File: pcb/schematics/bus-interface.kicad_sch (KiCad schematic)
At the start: 46 parts, among them J3 Conn_01x06, J4 Conn_01x06, U3 LCMXO2-1200HC-4TG100I

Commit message: add decoupling caps on bus controller
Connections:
- net +3V3: now also U3.93 (VCCIO0)
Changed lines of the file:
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@@
   (junction (at 82.55 44.45) (diameter 0) (color 0 0 0 0)
   )
+  (junction (at 134.62 36.83) (diameter 0) (color 0 0 0 0)
+  )
   (junction (at 241.3 49.53) (diameter 0) (color 0 0 0 0)
   )
@@
     (stroke (width 0) (type default))
   )
+  (wire (pts (xy 134.62 39.37) (xy 134.62 36.83))
+    (stroke (width 0) (type default))
+  )
   (wire (pts (xy 38.1 92.71) (xy 38.1 96.52))
     (stroke (width 0) (type default))
@@
     (stroke (width 0) (type default))
   )
-  (wire (pts (xy 133.35 36.83) (xy 149.86 36.83))
+  (wire (pts (xy 133.35 36.83) (xy 134.62 36.83))
     (stroke (width 0) (type default))
   )
@@
     (stroke (width 0) (type default))
   )
+  (wire (pts (xy 133.35 39.37) (xy 134.62 39.37))
+    (stroke (width 0) (type default))
+  )
   (wire (pts (xy 177.8 62.23) (xy 177.8 60.96))
     (stroke (width 0) (type default))
@@
     (stroke (width 0) (type default))
   )
+  (wire (pts (xy 134.62 36.83) (xy 149.86 36.83))
+    (stroke (width 0) (type default))
+  )

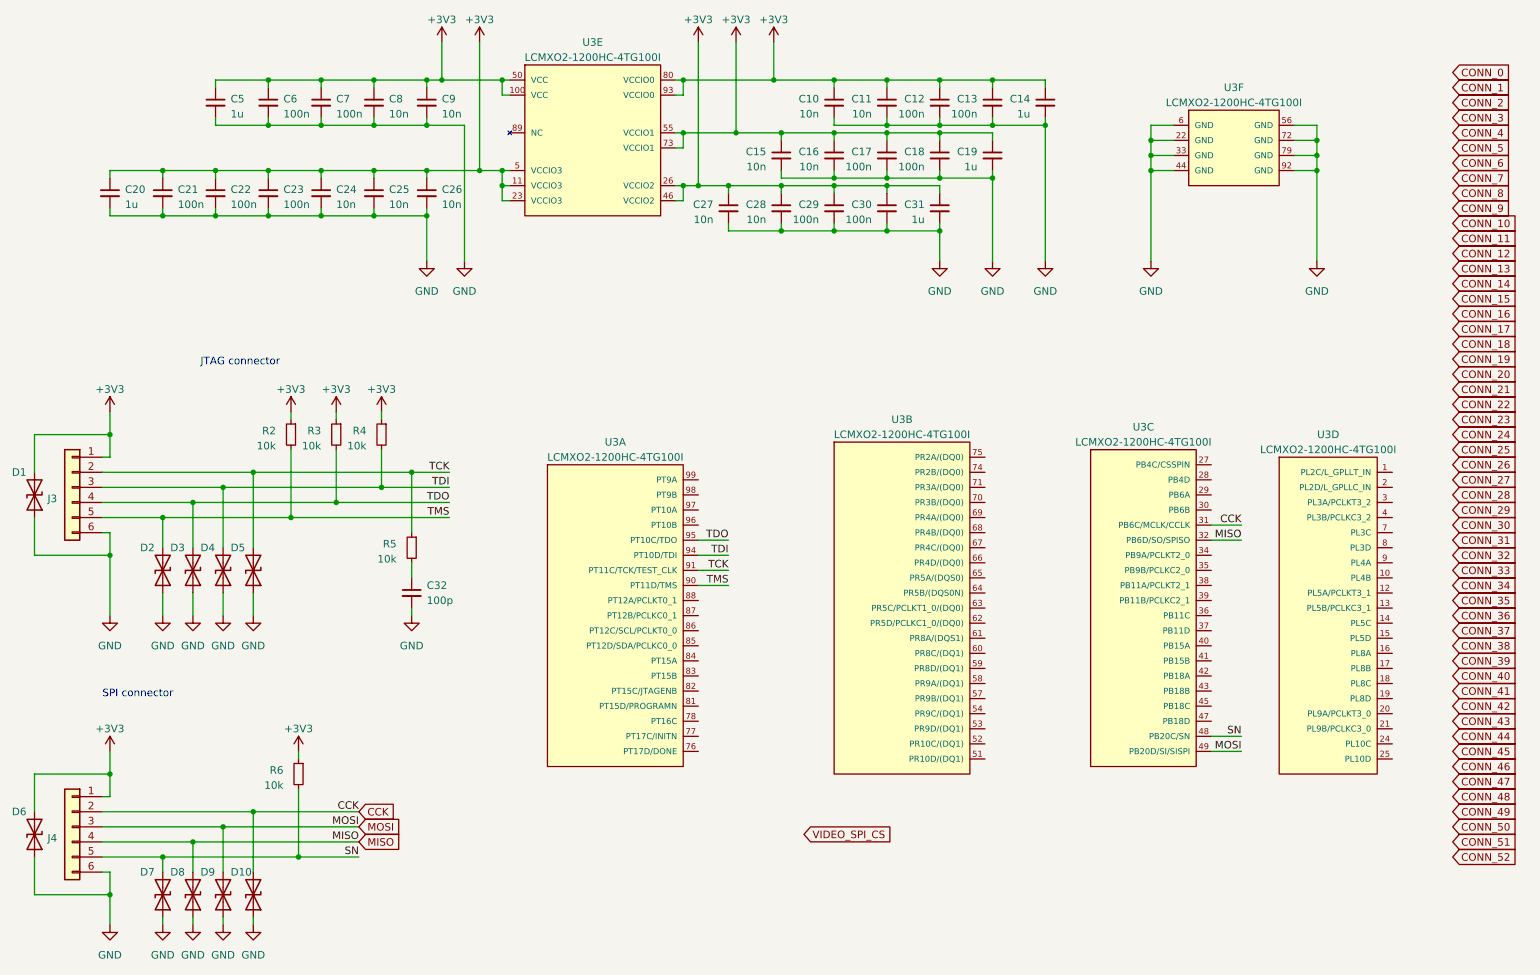
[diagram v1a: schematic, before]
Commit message: add traces from bus to bus controller
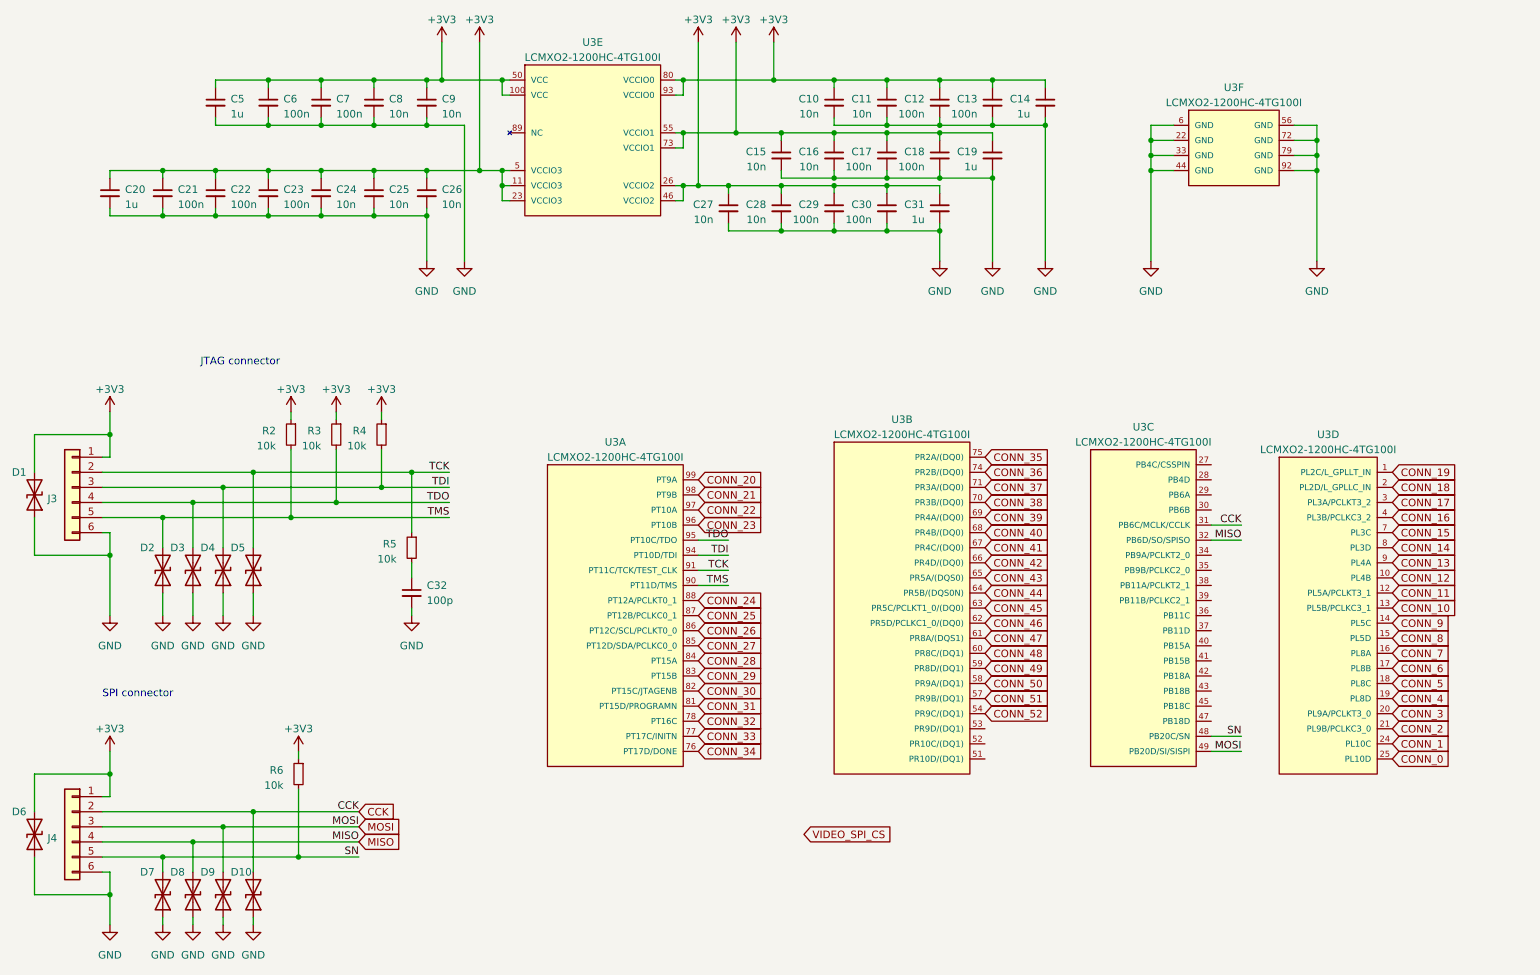
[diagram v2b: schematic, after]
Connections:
- net CONN_0: now also U3.25 (PL10D)
- net CONN_1: now also U3.24 (PL10C)
- net CONN_10: now also U3.13 (PL5B/PCLKC3_1)
- net CONN_11: now also U3.12 (PL5A/PCLKT3_1)
- net CONN_12: now also U3.10 (PL4B)
- net CONN_13: now also U3.9 (PL4A)
- net CONN_14: now also U3.8 (PL3D)
- net CONN_15: now also U3.7 (PL3C)
- net CONN_16: now also U3.4 (PL3B/PCLKC3_2)
- net CONN_17: now also U3.3 (PL3A/PCLKT3_2)
- net CONN_18: now also U3.2 (PL2D/L_GPLLC_IN)
- net CONN_19: now also U3.1 (PL2C/L_GPLLT_IN)
- net CONN_2: now also U3.21 (PL9B/PCLKC3_0)
- net CONN_20: now also U3.99 (PT9A)
- net CONN_21: now also U3.98 (PT9B)
- net CONN_22: now also U3.97 (PT10A)
- net CONN_23: now also U3.96 (PT10B)
- net CONN_24: now also U3.88 (PT12A/PCLKT0_1)
- net CONN_25: now also U3.87 (PT12B/PCLKC0_1)
- net CONN_26: now also U3.86 (PT12C/SCL/PCLKT0_0)
- net CONN_27: now also U3.85 (PT12D/SDA/PCLKC0_0)
- net CONN_28: now also U3.84 (PT15A)
- net CONN_29: now also U3.83 (PT15B)
- net CONN_3: now also U3.20 (PL9A/PCLKT3_0)
- net CONN_30: now also U3.82 (PT15C/JTAGENB)
- net CONN_31: now also U3.81 (PT15D/PROGRAMN)
- net CONN_32: now also U3.78 (PT16C)
- net CONN_33: now also U3.77 (PT17C/INITN)
- net CONN_34: now also U3.76 (PT17D/DONE)
- net CONN_35: now also U3.75 (PR2A/(DQ0))
- net CONN_36: now also U3.74 (PR2B/(DQ0))
- net CONN_37: now also U3.71 (PR3A/(DQ0))
- net CONN_38: now also U3.70 (PR3B/(DQ0))
- net CONN_39: now also U3.69 (PR4A/(DQ0))
- net CONN_4: now also U3.19 (PL8D)
- net CONN_40: now also U3.68 (PR4B/(DQ0))
- net CONN_41: now also U3.67 (PR4C/(DQ0))
- net CONN_42: now also U3.66 (PR4D/(DQ0))
- net CONN_43: now also U3.65 (PR5A/(DQS0))
- net CONN_44: now also U3.64 (PR5B/(DQS0N))
- net CONN_45: now also U3.63 (PR5C/PCLKT1_0/(DQ0))
- net CONN_46: now also U3.62 (PR5D/PCLKC1_0/(DQ0))
- net CONN_47: now also U3.61 (PR8A/(DQS1))
- net CONN_48: now also U3.60 (PR8C/(DQ1))
- net CONN_49: now also U3.59 (PR8D/(DQ1))
- net CONN_5: now also U3.18 (PL8C)
- net CONN_50: now also U3.58 (PR9A/(DQ1))
- net CONN_51: now also U3.57 (PR9B/(DQ1))
- net CONN_52: now also U3.54 (PR9C/(DQ1))
- net CONN_6: now also U3.17 (PL8B)
- net CONN_7: now also U3.16 (PL8A)
- net CONN_8: now also U3.15 (PL5D)
- net CONN_9: now also U3.14 (PL5C)

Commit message: add a unified programming connector
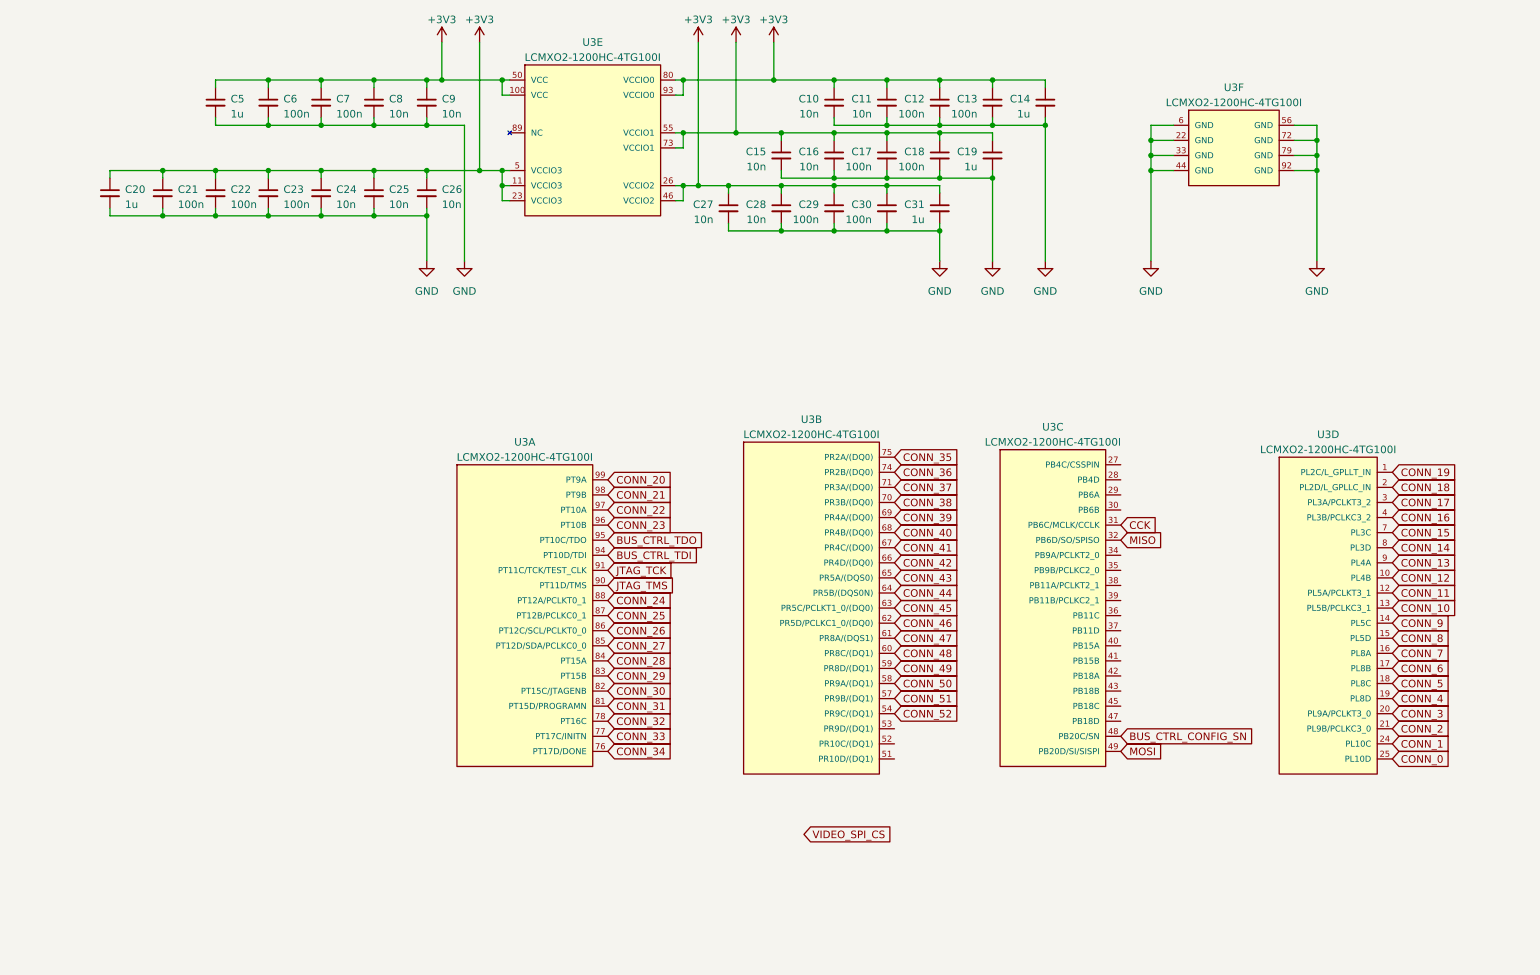
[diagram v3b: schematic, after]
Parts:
- removed C32: 100p, Capacitor_SMD:C_0402_1005Metric, symbol Device:C_Small
- removed D1, D10, D2, D3, D4, D5, D6, D7, D8, D9: D_TVS, Diode_SMD:D_0603_1608Metric, symbol Device:D_TVS
- removed J3, J4: Conn_01x06, Connector:Tag-Connect_TC2030-IDC-NL_2x03_P1.27mm_Vertical, symbol Connector_Generic:Conn_01x06
- removed R2, R3, R4, R5, R6: 10k, Resistor_SMD:R_0603_1608Metric, symbol Device:R_Small
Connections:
- net SN renamed BUS_CTRL_CONFIG_SN
- net TCK renamed JTAG_TCK
- net TDI renamed BUS_CTRL_TDI
- net TDO renamed BUS_CTRL_TDO
- net TMS renamed JTAG_TMS
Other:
- note removed: "JTAG connector"
- note removed: "SPI connector"
- moved on the sheet: U3A, U3B, U3C

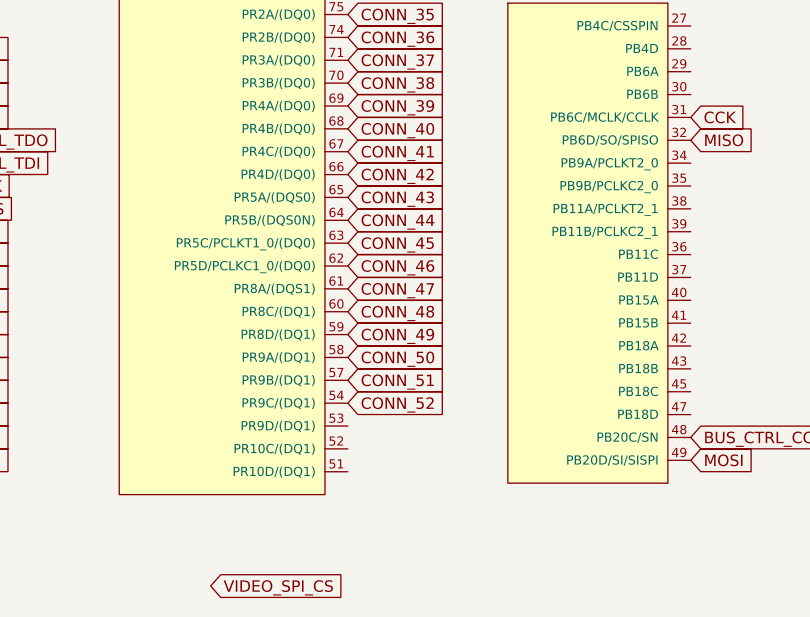
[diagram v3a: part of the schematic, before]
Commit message: add the 3v3 voltage regulator
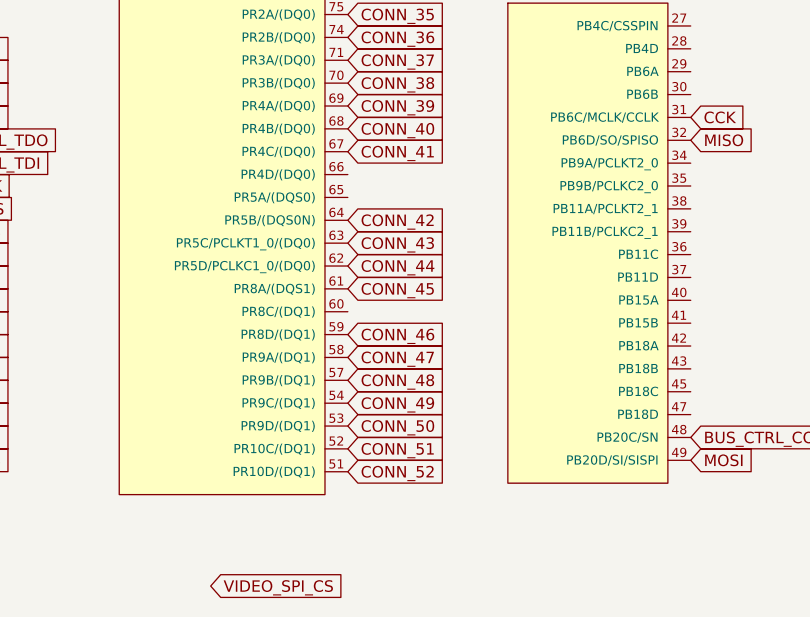
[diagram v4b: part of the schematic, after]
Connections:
- net CONN_42: now also U3.64 (PR5B/(DQS0N)); no longer U3.66 (PR4D/(DQ0))
- net CONN_43: now also U3.63 (PR5C/PCLKT1_0/(DQ0)); no longer U3.65 (PR5A/(DQS0))
- net CONN_44: now also U3.62 (PR5D/PCLKC1_0/(DQ0)); no longer U3.64 (PR5B/(DQS0N))
- net CONN_45: now also U3.61 (PR8A/(DQS1)); no longer U3.63 (PR5C/PCLKT1_0/(DQ0))
- net CONN_46: now also U3.59 (PR8D/(DQ1)); no longer U3.62 (PR5D/PCLKC1_0/(DQ0))
- net CONN_47: now also U3.58 (PR9A/(DQ1)); no longer U3.61 (PR8A/(DQS1))
- net CONN_48: now also U3.57 (PR9B/(DQ1)); no longer U3.60 (PR8C/(DQ1))
- net CONN_49: now also U3.54 (PR9C/(DQ1)); no longer U3.59 (PR8D/(DQ1))
- net CONN_50: now also U3.53 (PR9D/(DQ1)); no longer U3.58 (PR9A/(DQ1))
- net CONN_51: now also U3.52 (PR10C/(DQ1)); no longer U3.57 (PR9B/(DQ1))
- net CONN_52: now also U3.51 (PR10D/(DQ1)); no longer U3.54 (PR9C/(DQ1))

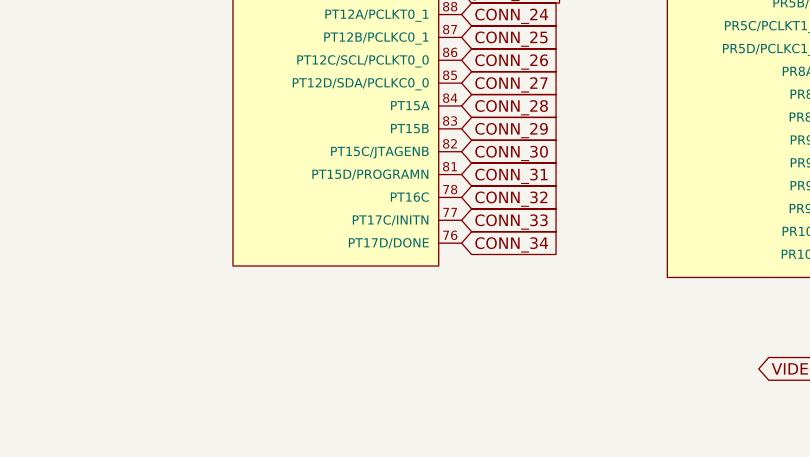
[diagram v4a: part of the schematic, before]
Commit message: add the programming controller
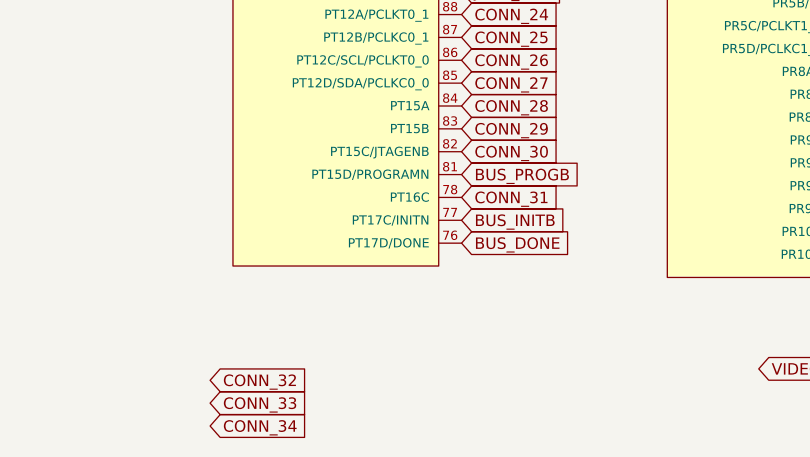
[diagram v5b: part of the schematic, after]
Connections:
- net CONN_31: now also U3.78 (PT16C); no longer U3.81 (PT15D/PROGRAMN)
- net CONN_32: no longer U3.78 (PT16C)
- net CONN_33: no longer U3.77 (PT17C/INITN)
- net CONN_34: no longer U3.76 (PT17D/DONE)
- new net BUS_DONE: U3.76 (PT17D/DONE)
- new net BUS_INITB: U3.77 (PT17C/INITN)
- new net BUS_PROGB: U3.81 (PT15D/PROGRAMN)
